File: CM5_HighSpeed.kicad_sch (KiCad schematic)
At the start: 19 parts, among them J10 690-019-298-412, J12 USB3_A, J16 Conn_01x22_Female, J22 690-019-298-412, J5 Conn_01x22_Female, J6 THD-02-R, U12 RT9742SNGV, U6 AP22653W6

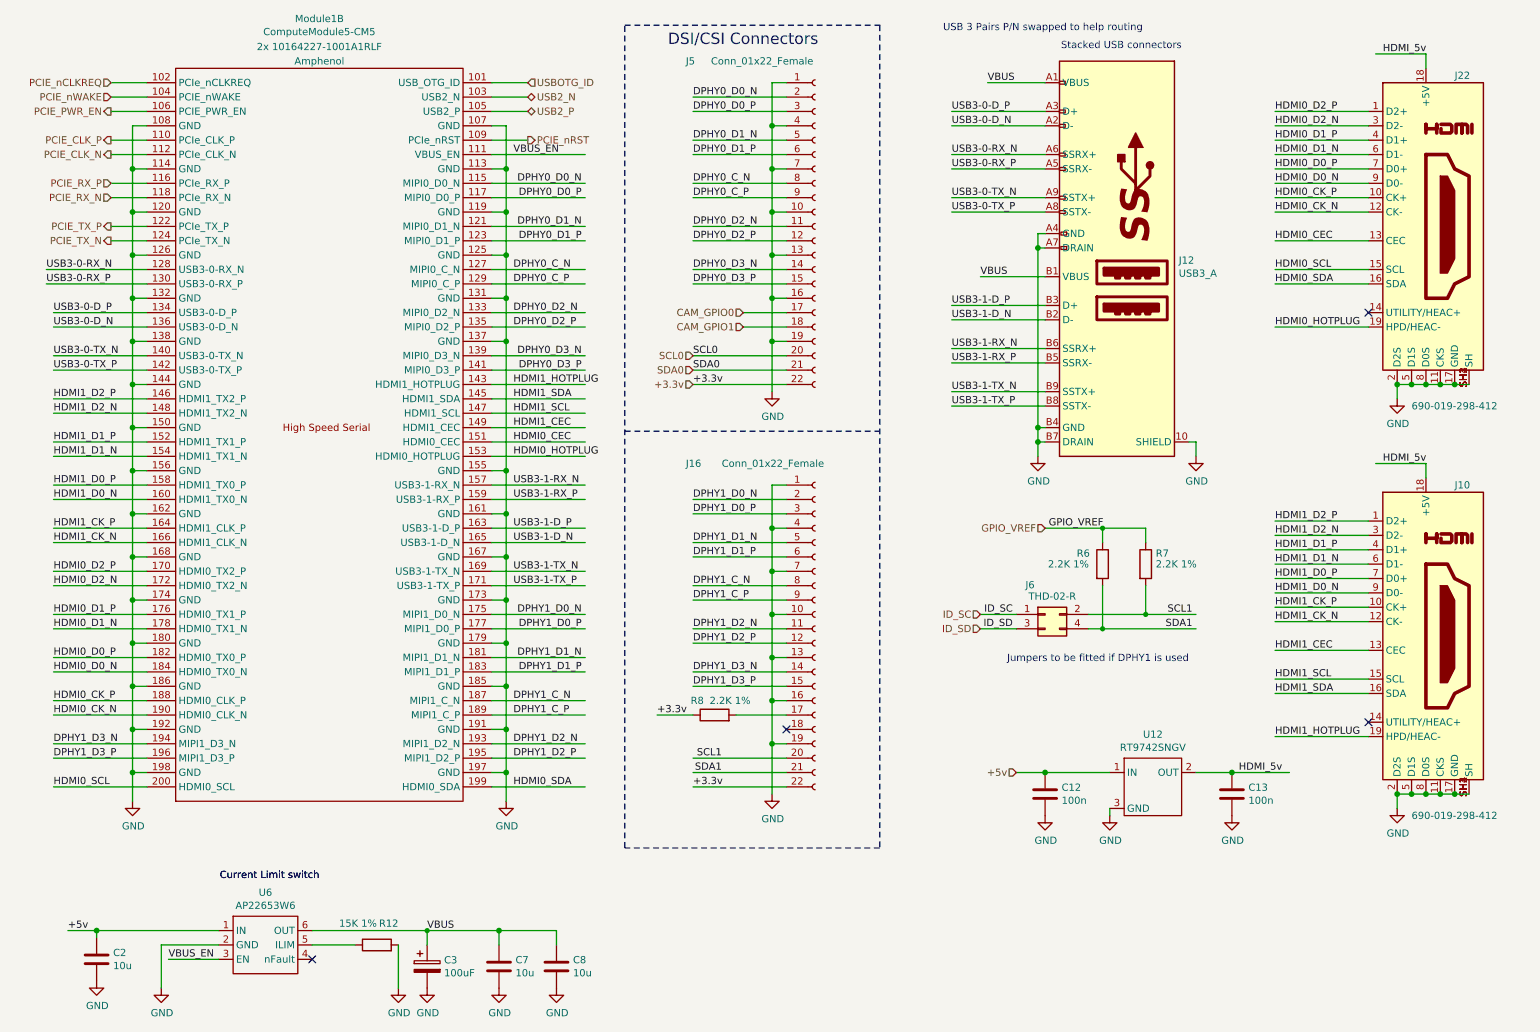
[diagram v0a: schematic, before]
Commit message: Removing unwanted sections, such that the carrier board is a blank canvas
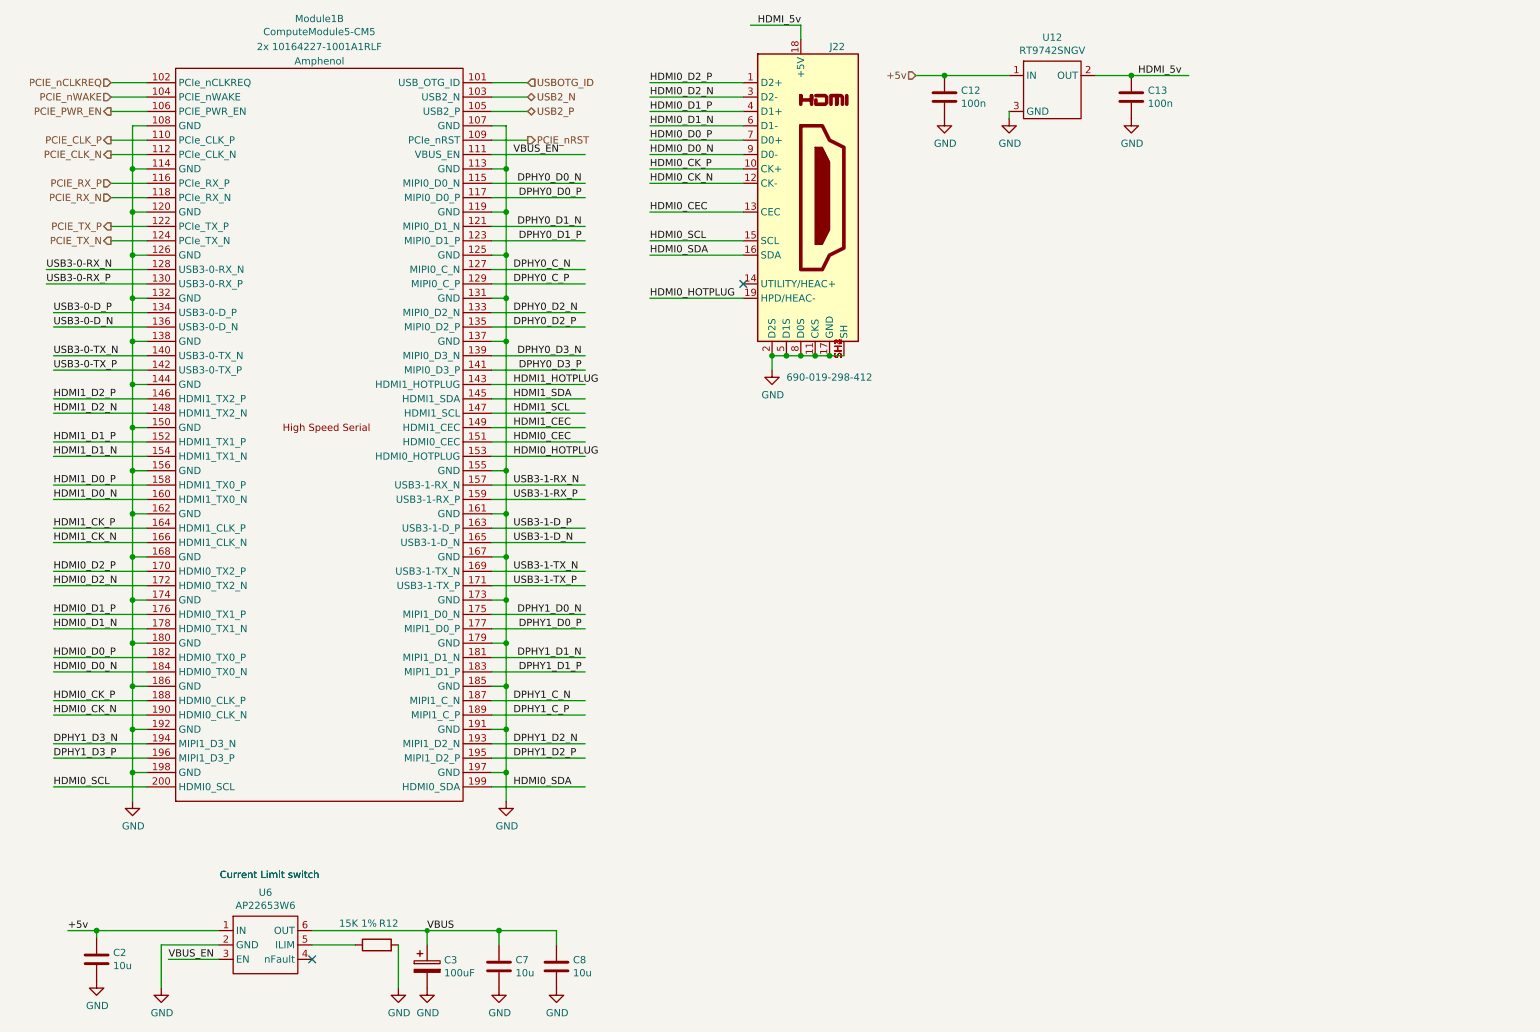
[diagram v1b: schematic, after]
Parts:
- removed J10: 690-019-298-412, CM5IO:EDAC 690-019-298-412, symbol CM5IO:HDMI_A_1.4
- removed J12: USB3_A, CM5IO:MTCONN_UBAF30-D2011, symbol CM5IO:USB3_A
- removed J16, J5: Conn_01x22_Female, CM5IO:Hirose_FH12-22S-0.5SH_1x22-1MP_P0.50mm_Horizontal, symbol Connector:Conn_01x22_Socket
- removed J6: THD-02-R, Connector_PinHeader_2.54mm:PinHeader_2x02_P2.54mm_Vertical, symbol Connector_Generic:Conn_02x02_Odd_Even
- removed R6, R7, R8: 2.2K 1%, Resistor_SMD:R_0402_1005Metric, symbol Device:R
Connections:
- no-connect marks 4 -> 2
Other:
- note removed: "DSI/CSI Connectors"
- note removed: "Jumpers to be fitted if DPHY1 is used"
- note removed: "Stacked USB connectors"
- note removed: "USB 3 Pairs P/N swapped to help routing"
- moved on the sheet: C12, C13, J22, U12

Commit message: Board development
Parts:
- added J5: USB3_A, CM5IO:MTCONN_UBAF30-D2011, symbol CM5IO:USB3_A
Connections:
- net GND: now also J5.A4 (GND), J5.A7 (DRAIN), J5.B4 (GND), J5.B7 (DRAIN)
- net USB3-0-D_N: now also J5.A2 (D-)
- net USB3-0-D_P: now also J5.A3 (D+)
- net USB3-0-RX_N: now also J5.A6 (SSRX+)
- net USB3-0-RX_P: now also J5.A5 (SSRX-)
- net USB3-0-TX_N: now also J5.A9 (SSTX+)
- net USB3-0-TX_P: now also J5.A8 (SSTX-)
- net USB3-1-D_N: now also J5.B2 (D-)
- net USB3-1-D_P: now also J5.B3 (D+)
- net USB3-1-RX_N: now also J5.B6 (SSRX+)
- net USB3-1-RX_P: now also J5.B5 (SSRX-)
- net USB3-1-TX_N: now also J5.B9 (SSTX+)
- net USB3-1-TX_P: now also J5.B8 (SSTX-)
- net VBUS: now also J5.A1 (VBUS), J5.B1 (VBUS)
